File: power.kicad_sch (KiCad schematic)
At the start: 25 parts, among them IC2 MPM3833CGRH-Z, IC5 BQ24074RGTR, IC6 LP2985-30DBVR, U1 NC7SVU04P5X, U2 NC7SVU04P5X

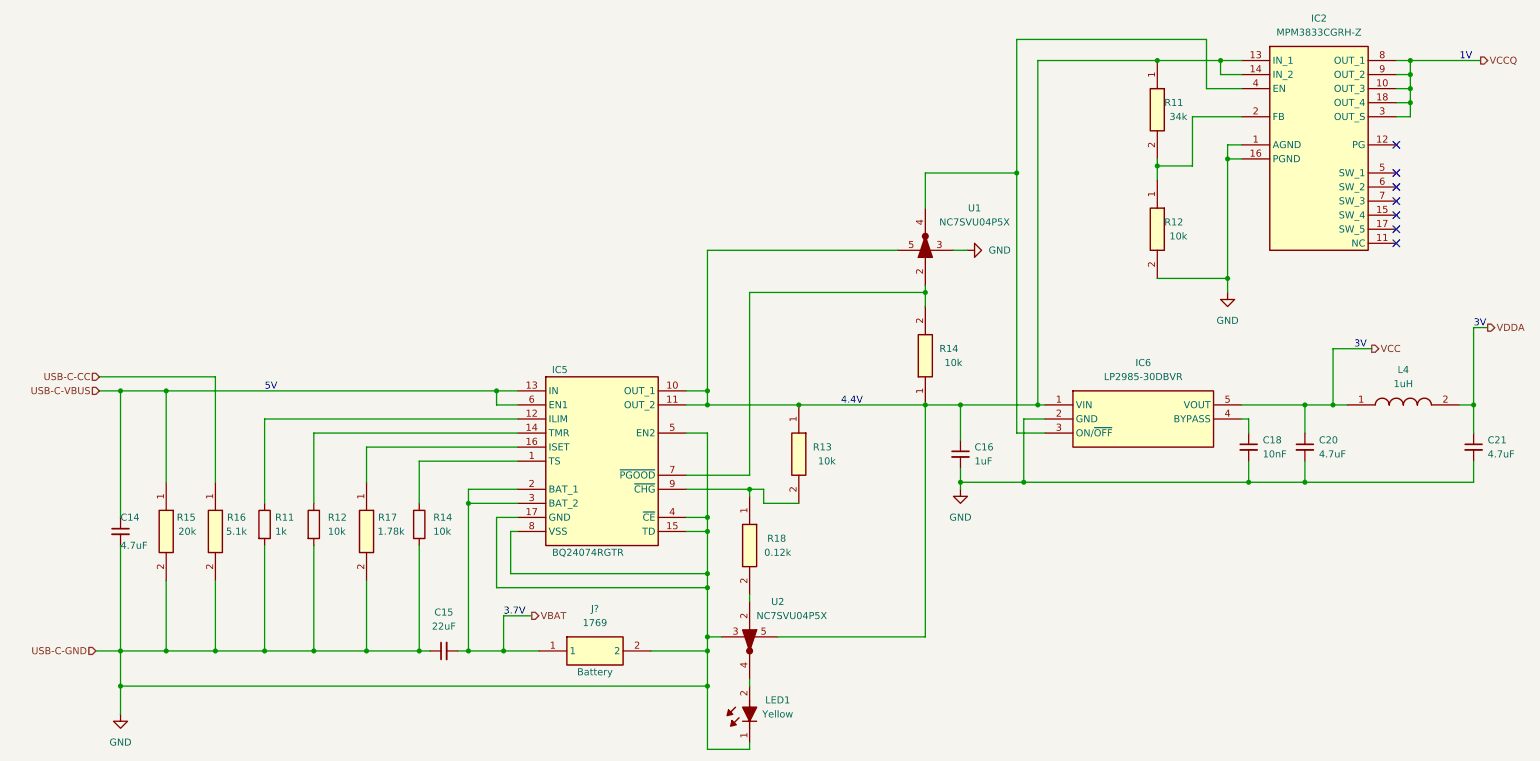
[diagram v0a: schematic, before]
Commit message: Updated KiCad Version of files
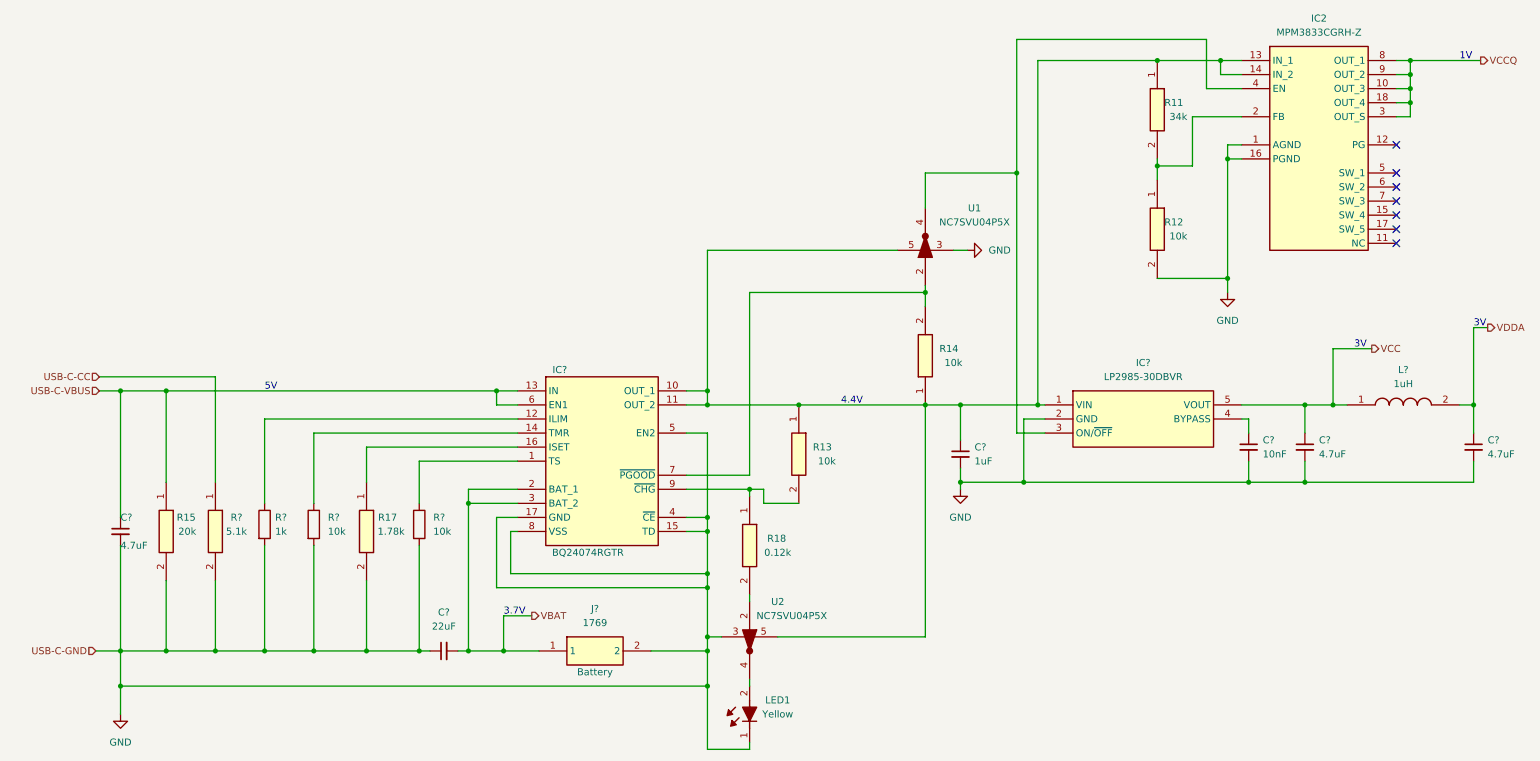
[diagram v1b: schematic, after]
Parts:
- renumbered C16 to C?, C15 to C?, C20 to C?, C21 to C?, C14 to C?, C18 to C?, IC6 to IC?, IC5 to IC?, L4 to L?, R16 to R?, R11 to R?, R12 to R?, R14 to R?
